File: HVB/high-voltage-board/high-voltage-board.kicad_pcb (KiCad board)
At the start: 2 copper layers, 181.6 x 106 mm, 76 parts, among them J1 Conn_01x23, J10 Conn_01x05, J11 HV-, J2 HECS, J3 HV+, J4 HV-, J5 HV+, J6 HV-, J7 Conn_01x02, J8 HV+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

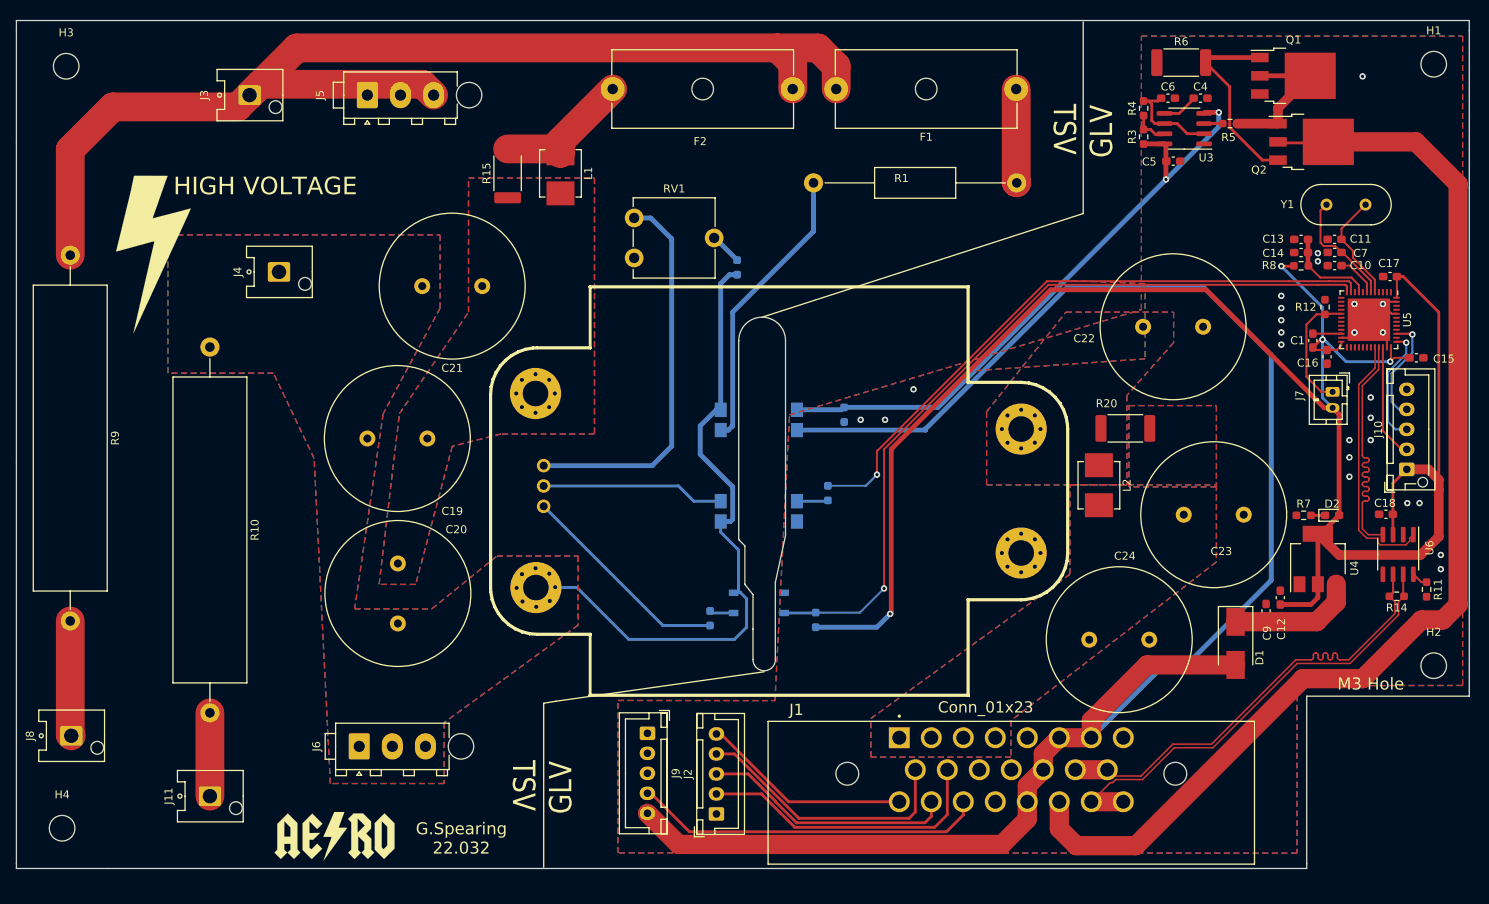
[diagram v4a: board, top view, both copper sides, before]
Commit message: updating footprint and 3d model links
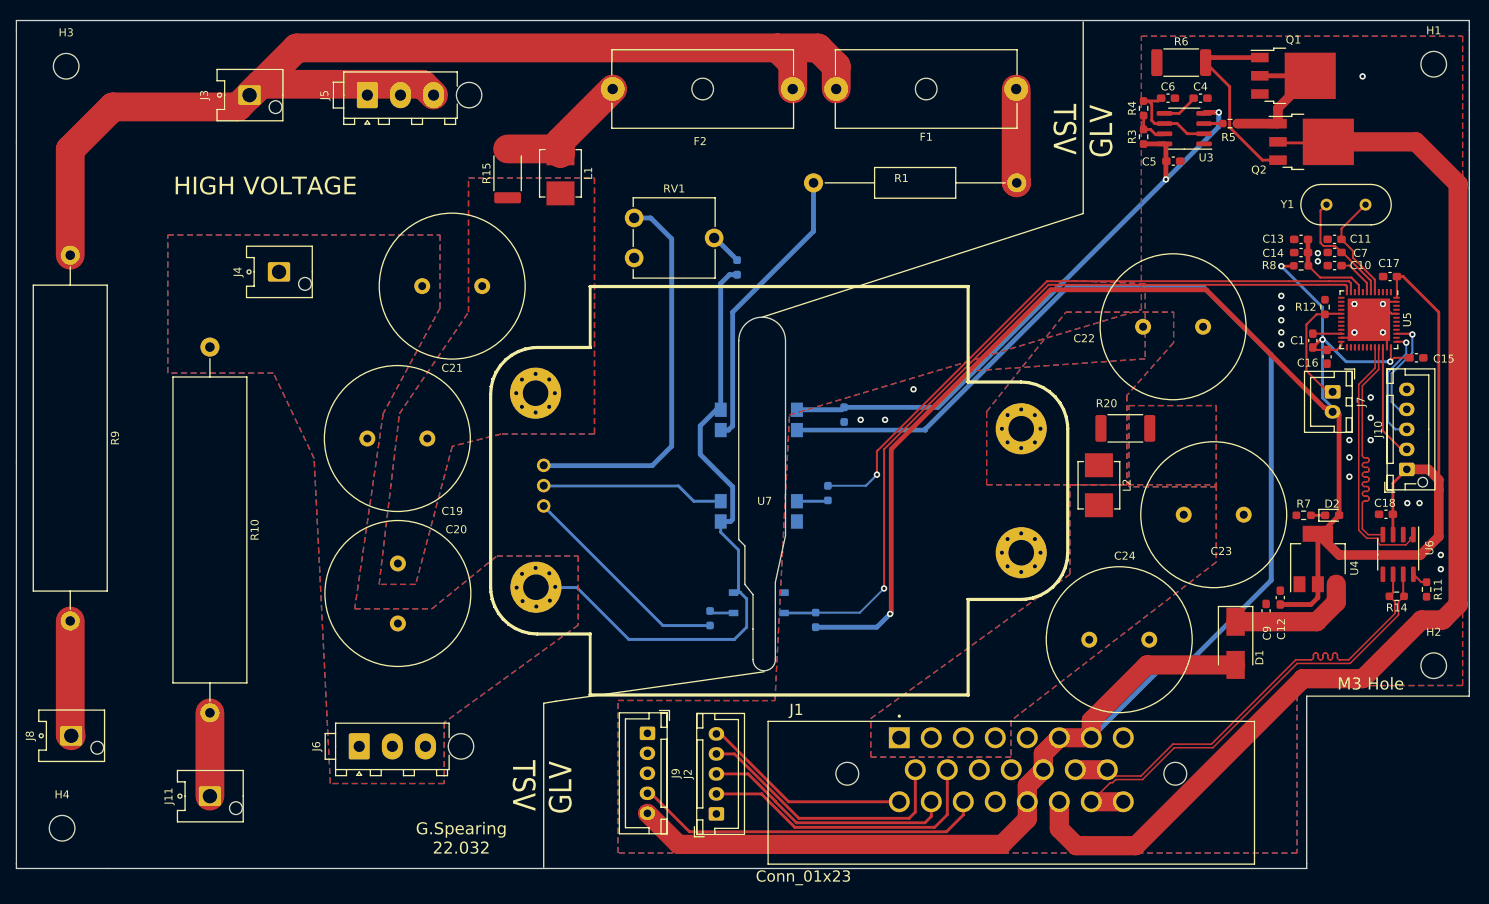
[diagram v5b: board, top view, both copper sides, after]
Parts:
- removed G*** (x2): LOGO, AERO_Footprints:hvlightningsymbol
- removed G***: LOGO, AERO_Footprints:AERO_Logo_15x6mm
- J1: footprint AERO_Footprints:TE_1-776087-1 -> AERO_Footprints:TE_1-770669-1_23pin_Horizontal
- J5, J6: footprint Connector_TE-Connectivity:TE_MATE-N-LOK_1-770870-x_1x03_P4.14mm_Vertical -> AERO_Footprints:TE_MATE-N-LOK_1-770870-x_1x03_P4.14mm_Vertical
- J7: footprint Connector_JST:JST_PH_B2B-PH-K_1x02_P2.00mm_Vertical -> Connector_JST:JST_XH_B2B-XH-A_1x02_P2.50mm_Vertical
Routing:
- net /TEMP-: track 15.5 -> 14.8 mm

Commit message: Layout and Footprints update
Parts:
- added G***: LOGO, AERO_Footprints:AERO_Logo_10x4mm, F.Cu at (205.7, 134.6)
- Q1, Q2: value 040N03LG -> PSMN5R2-60YL; footprint Package_TO_SOT_SMD:TO-252-3_TabPin2 -> Package_TO_SOT_SMD:LFPAK56
- moved J7 3.75 mm to (212.2, 88.9)
- moved J9 3.13 mm to (123.4, 127.8)
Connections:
- net /vicor/TRIM_HV renamed /DC_DC_TRIM_EN
- Q1 pad 1: Net-(Q1-Pad1) -> GND
- Q1 pad 2: Net-(Q1-Pad2) -> GND
- Q2 pad 1: Net-(Q1-Pad2) -> Net-(R6-Pad2)
- Q2 pad 2: /TSAL_GND -> Net-(R6-Pad2)
- Q2 pad 3: Net-(Q1-Pad1) -> Net-(R6-Pad2)
- R5 pad 1: Net-(Q1-Pad2) -> Net-(R5-Pad1)
- R6 pad 2: Net-(Q1-Pad1) -> Net-(R6-Pad2)
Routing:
- net Net-(Q1-Pad1): track 24.1 -> 0.00 mm
- net Net-(R5-Pad1): track 0.00 -> 19.8 mm
- net Net-(Q1-Pad2): track 19.0 -> 0.00 mm
- net Net-(R6-Pad2): track 0.00 -> 17.7 mm, vias 0 -> 2
- net /TSAL_GND: track 143.9 -> 137.6 mm
- net +3V3: track 242.5 -> 247.5 mm
- net /TEMP-: track 14.8 -> 18.4 mm
- net /IMD_OK: track 43.5 -> 46.7 mm
- net +12V: track 218.4 -> 221.6 mm
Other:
- board text added: "12V"
- board text added: "3.3V"
- board text added: "5V"
- board text added: "AN1"
- board text added: "AN2"
- board text added: "AN3"
- board text added: "CLK"
- board text added: "DIO"
- board text added: "GND"
- board text added: "HV+"
- board text added: "HV-"
- board text added: "IMD_OK"
- board text added: "TEMP"
- board text added: "TSMP+"
- board text added: "TSMP-"
- board text added: "Trace"

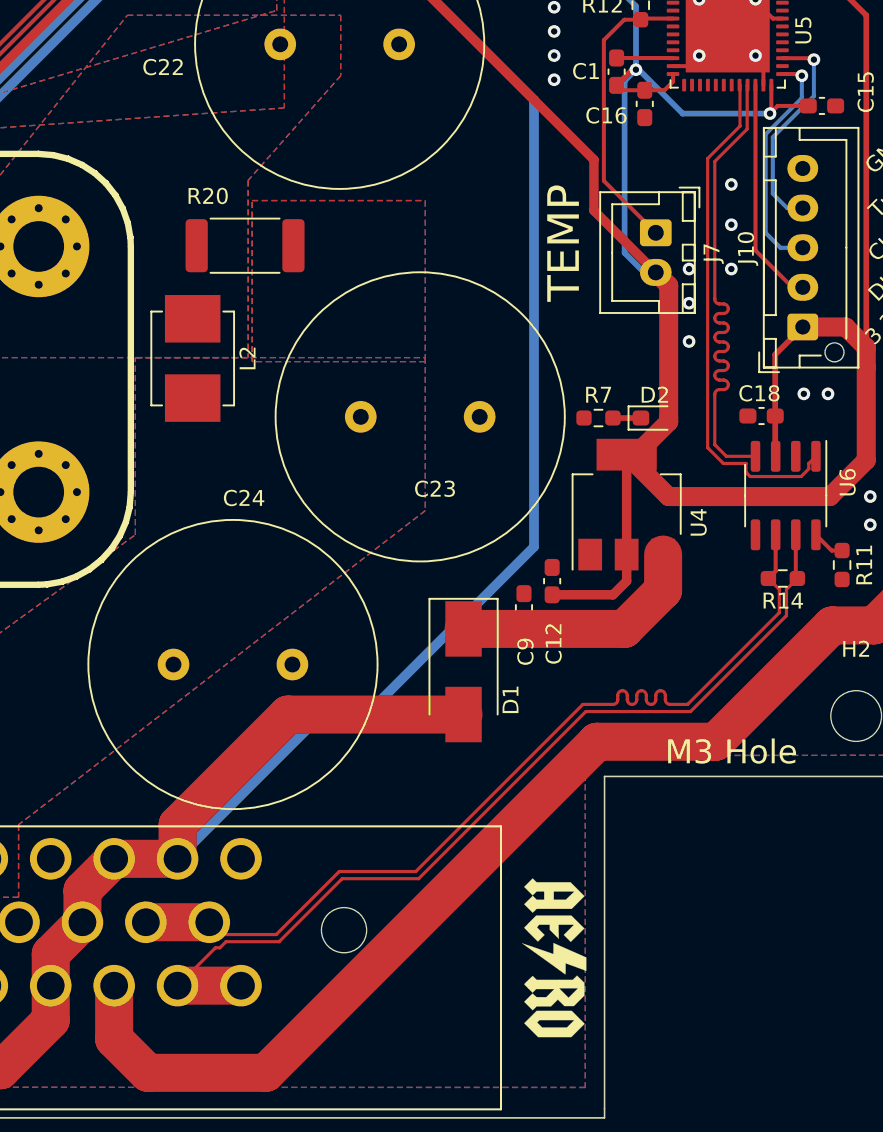
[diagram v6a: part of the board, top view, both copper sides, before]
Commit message: updating can pinouts
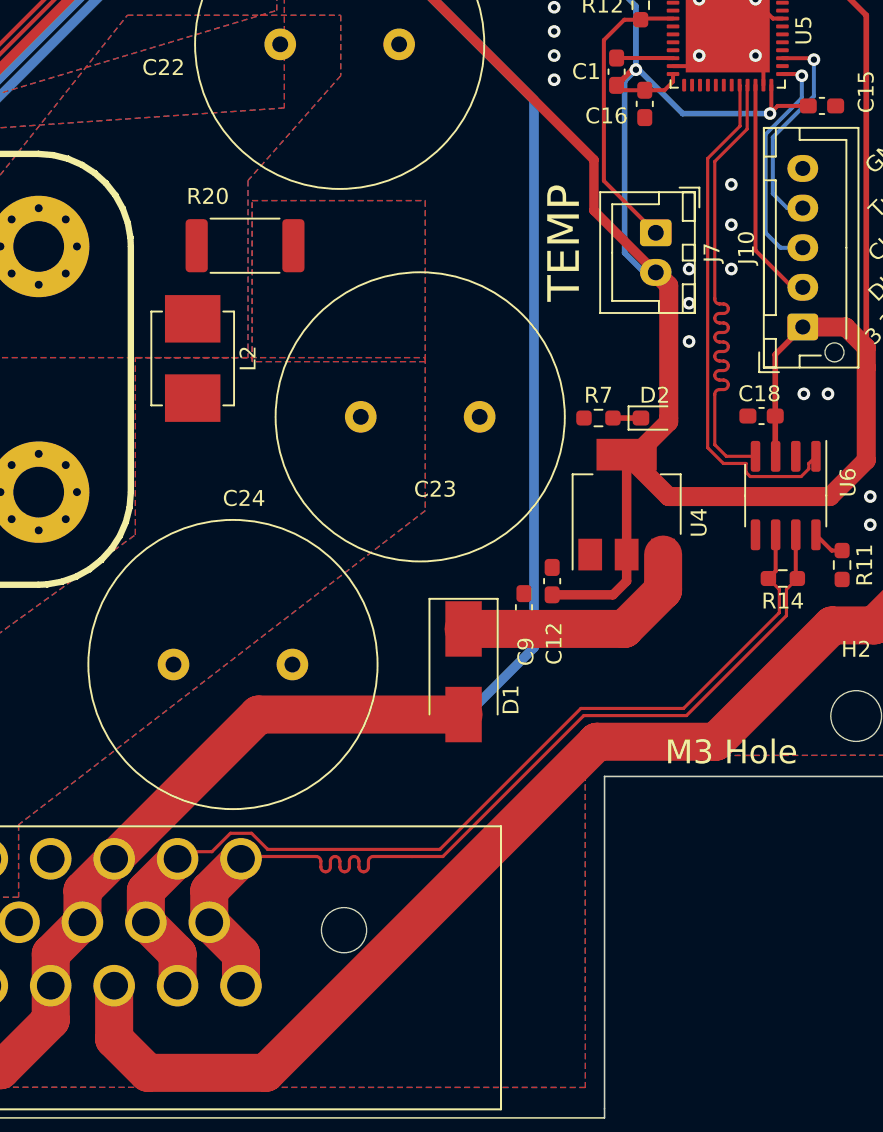
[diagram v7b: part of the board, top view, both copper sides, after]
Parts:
- removed G***: LOGO, AERO_Footprints:AERO_Logo_10x4mm
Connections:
- J1 pad 15: /CAN- -> /CAN+
- J1 pad 22: /CAN+ -> /CAN-
- J1 pad 7: +12V -> /CAN-
- J1 pad 8: GND -> /CAN+
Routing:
- net +12V: track 221.6 -> 228.0 mm
- net /CAN-: track 57.6 -> 60.3 mm
- net /CAN+: track 57.5 -> 59.9 mm
